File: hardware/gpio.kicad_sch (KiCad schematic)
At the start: 13 parts, among them U4 CCGM1A1

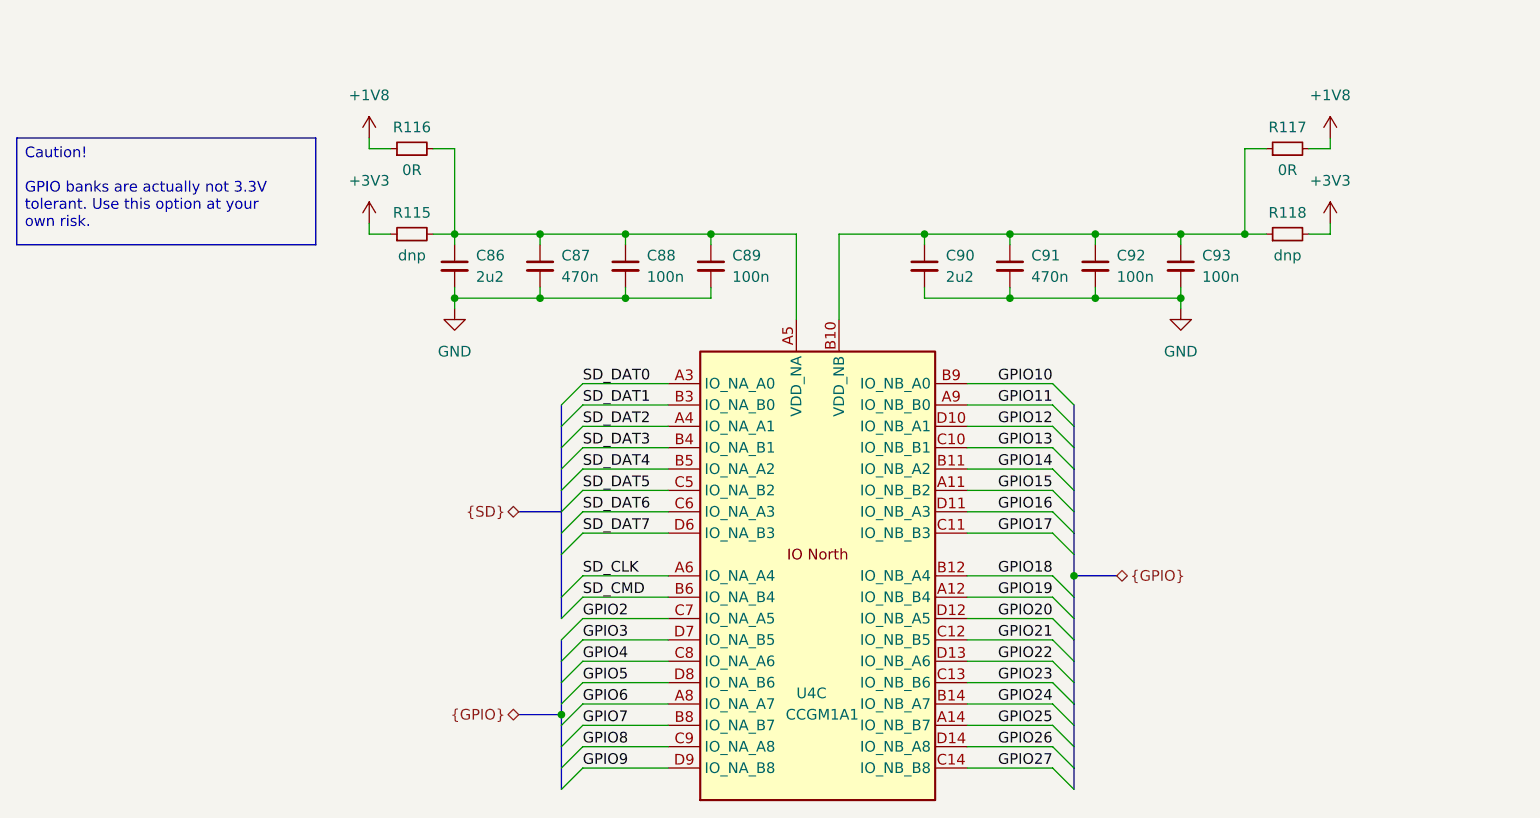
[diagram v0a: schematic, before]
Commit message: Using high SDcard pins for SDRAM
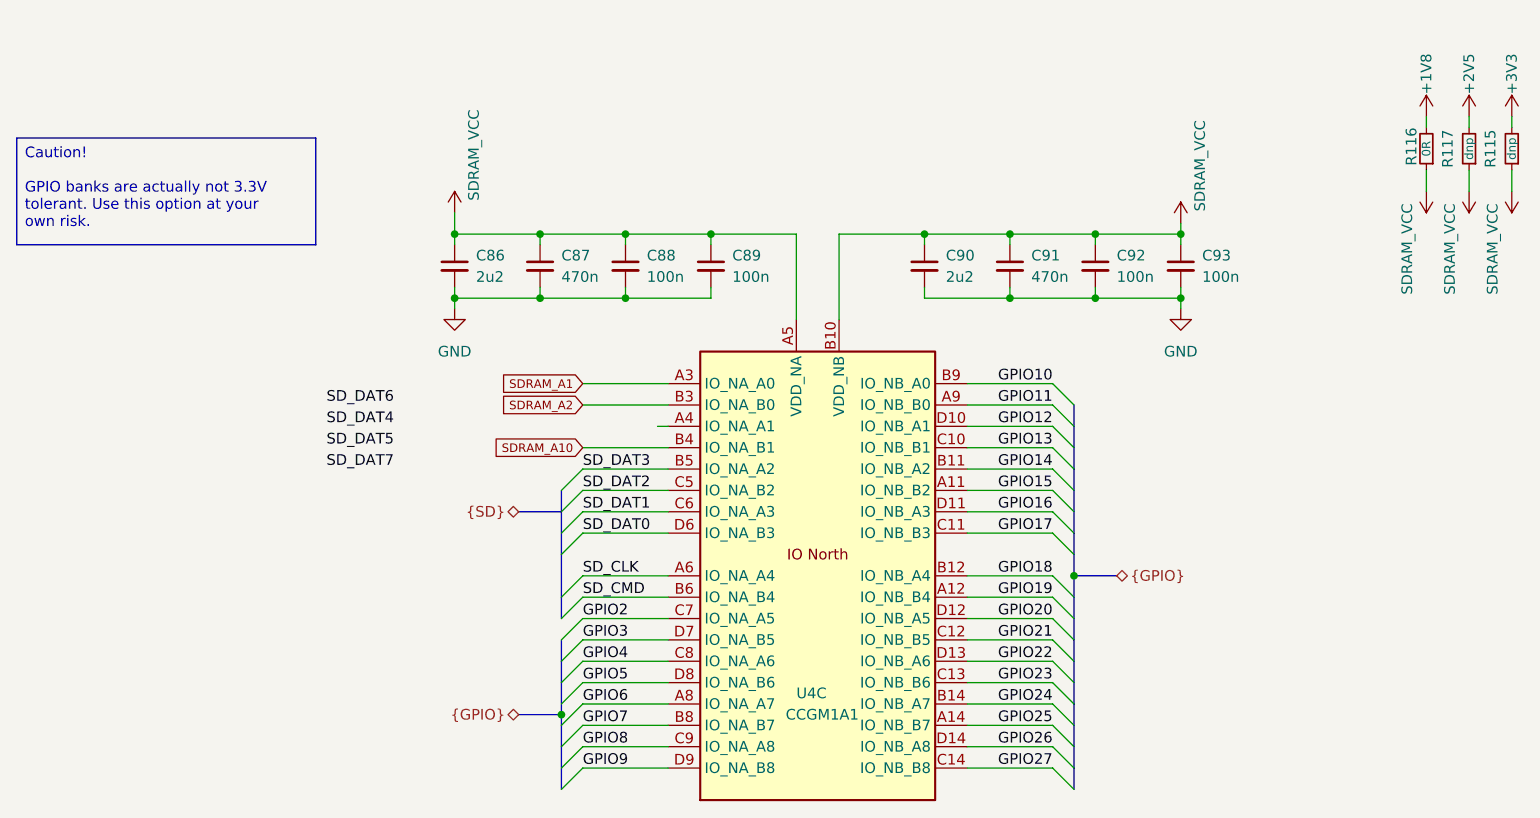
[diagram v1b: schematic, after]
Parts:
- removed R118: dnp, Resistor_SMD:R_0402_1005Metric, symbol Device:R_Small
- R117: value 0R -> dnp
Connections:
- net +1V8: now also R116.2; no longer R116.1, R117.2
- net +3V3: now also R115.2; no longer R115.1
- net SD_DAT0: now also U4.D6 (IO_NA_B3); no longer U4.A3 (IO_NA_A0)
- net SD_DAT1: now also U4.C6 (IO_NA_A3); no longer U4.B3 (IO_NA_B0)
- net SD_DAT2: now also U4.C5 (IO_NA_B2); no longer U4.A4 (IO_NA_A1)
- net SD_DAT3: now also U4.B5 (IO_NA_A2); no longer U4.B4 (IO_NA_B1)
- net SD_DAT4: no longer U4.B5 (IO_NA_A2)
- net SD_DAT5: no longer U4.C5 (IO_NA_B2)
- net SD_DAT6: no longer U4.C6 (IO_NA_A3)
- net SD_DAT7: no longer U4.D6 (IO_NA_B3)
- net SDRAM_VCC: now reaches C90.1, C91.1, C92.1, C93.1, R117.1, U4.B10 (VDD_NB), U4.B13 (VDD_NB), U4.E10 (VDD_NB), U4.E12 (VDD_NB), U4.F11 (VDD_NB)
- net SDRAM_VCC: now also C86.1, C87.1, C88.1, C89.1, R115.1, R116.1, U4.A5 (VDD_NA), U4.B7 (VDD_NA), U4.E6 (VDD_NA), U4.E8 (VDD_NA), U4.F7 (VDD_NA)
- new net +2V5: R117.2
- new net SDRAM_A1: U4.A3 (IO_NA_A0)
- new net SDRAM_A10: U4.B4 (IO_NA_B1)
- new net SDRAM_A2: U4.B3 (IO_NA_B0)
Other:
- moved on the sheet: R115, R116

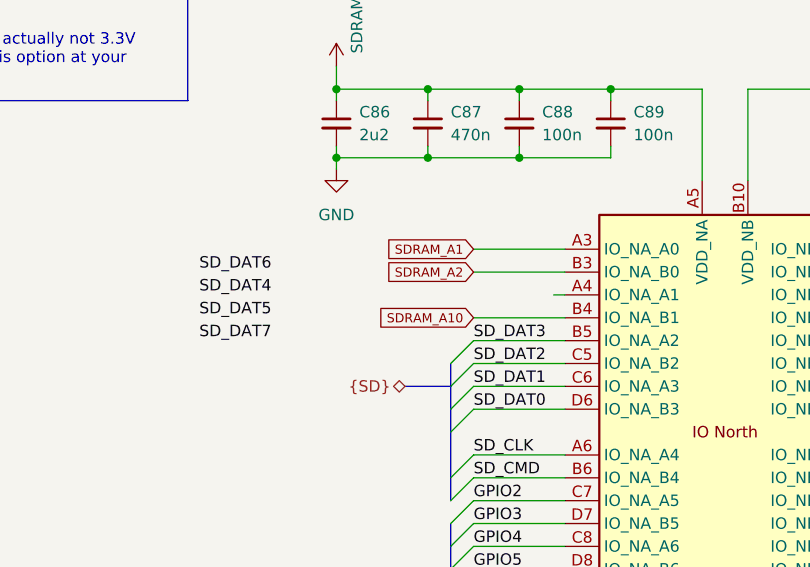
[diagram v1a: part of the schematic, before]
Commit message: Adding USB connector and level converter
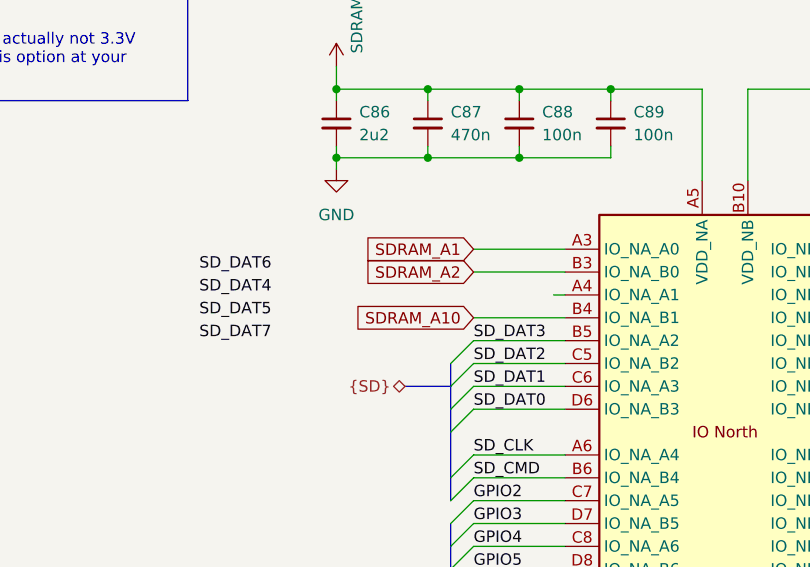
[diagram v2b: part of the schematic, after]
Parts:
- U4: footprint Package_BGA:BGA-324_15.0x15.0mm_Layout18x18_P0.8mm_Ball0.45mm_Pad0.4mm_NSMD -> ulx5m-gs:BGA-324_15.0x15.0mm_Layout18x18_P0.8mm_Ball0.45mm_Pad0.4mm_NSMD
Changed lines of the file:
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@@
 		(effects
 			(font
-				(size 1.016 1.016)
+				(size 1.27 1.27)
 			)
 			(justify right)
@@
 		(effects
 			(font
-				(size 1.016 1.016)
+				(size 1.27 1.27)
 			)
 			(justify right)
@@
 		(effects
 			(font
-				(size 1.016 1.016)
+				(size 1.27 1.27)
 			)
 			(justify right)
@@
 			)
 		)
-		(property "Footprint" "Package_BGA:BGA-324_15.0x15.0mm_Layout18x18_P0.8mm_Ball0.45mm_Pad0.4mm_NSMD"
+		(property "Footprint" "ulx5m-gs:BGA-324_15.0x15.0mm_Layout18x18_P0.8mm_Ball0.45mm_Pad0.4mm_NSMD"
 			(at 147.32 62.23 0)
 			(effects

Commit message: Routing diff clock
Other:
- company: (none) -> ${project_creator}
- title: (none) -> ${project_name}
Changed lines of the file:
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@@
 	(generator_version "9.0")
 	(paper "A4")
+	(title_block
+		(title "${project_name}")
+		(date "2025-06-24")
+		(rev "${project_version}")
+		(company "${project_creator}")
+		(comment 1 "${project_license}")
+	)
 	(text_box "Caution!\n\nGPIO banks are actually not 3.3V tolerant. Use this option at your own risk."
 		(exclude_from_sim no)

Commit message: Clearing errors
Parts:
- added R126, R127: 4R7, Resistor_SMD:R_0402_1005Metric, symbol Device:R_Small
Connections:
- net SDRAM_VCC: now also R126.1, R127.2; no longer C87.1, C88.1, C89.1, C90.1, C91.1, C92.1, U4.A5 (VDD_NA), U4.B10 (VDD_NB), U4.B13 (VDD_NB), U4.B7 (VDD_NA), U4.E10 (VDD_NB), U4.E12 (VDD_NB), U4.E6 (VDD_NA), U4.E8 (VDD_NA), U4.F11 (VDD_NB), U4.F7 (VDD_NA)
- new net VCC_NA: C87.1, C88.1, C89.1, R126.2, U4.A5 (VDD_NA), U4.B7 (VDD_NA), U4.E6 (VDD_NA), U4.E8 (VDD_NA), U4.F7 (VDD_NA)
- new net VCC_NB: C90.1, C91.1, C92.1, R127.1, U4.B10 (VDD_NB), U4.B13 (VDD_NB), U4.E10 (VDD_NB), U4.E12 (VDD_NB), U4.F11 (VDD_NB)
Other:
- moved on the sheet: R115, R116, R117

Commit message: Routing GPIO
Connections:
- net GPIO10: now also U4.C10 (IO_NB_B1); no longer U4.B9 (IO_NB_A0)
- net GPIO11: now also U4.C11 (IO_NB_B3); no longer U4.A9 (IO_NB_B0)
- net GPIO12: now also U4.A12 (IO_NB_B4); no longer U4.D10 (IO_NB_A1)
- net GPIO13: now also U4.D13 (IO_NB_A6); no longer U4.C10 (IO_NB_B1)
- net GPIO14: now also U4.A6 (IO_NA_A4); no longer U4.B11 (IO_NB_A2)
- net GPIO15: now also U4.B6 (IO_NA_B4); no longer U4.A11 (IO_NB_B2)
- net GPIO16: now also U4.B12 (IO_NB_A4); no longer U4.D11 (IO_NB_A3)
- net GPIO17: now also U4.C8 (IO_NA_A6); no longer U4.C11 (IO_NB_B3)
- net GPIO18: now also U4.A8 (IO_NA_A7); no longer U4.B12 (IO_NB_A4)
- net GPIO19: now also U4.C14 (IO_NB_B8); no longer U4.A12 (IO_NB_B4)
- net GPIO2: now also U4.D7 (IO_NA_B5); no longer U4.C7 (IO_NA_A5)
- net GPIO20: now also U4.A14 (IO_NB_B7); no longer U4.D12 (IO_NB_A5)
- net GPIO21: now also U4.B14 (IO_NB_A7); no longer U4.C12 (IO_NB_B5)
- net GPIO22: now also U4.D9 (IO_NA_B8); no longer U4.D13 (IO_NB_A6)
- net GPIO23: now also U4.B8 (IO_NA_B7); no longer U4.C13 (IO_NB_B6)
- net GPIO24: now also U4.A9 (IO_NB_B0); no longer U4.B14 (IO_NB_A7)
- net GPIO25: now also U4.B9 (IO_NB_A0); no longer U4.A14 (IO_NB_B7)
- net GPIO27: now also U4.C9 (IO_NA_A8); no longer U4.C14 (IO_NB_B8)
- net GPIO3: now also U4.C7 (IO_NA_A5); no longer U4.D7 (IO_NA_B5)
- net GPIO4: now also U4.D8 (IO_NA_B6); no longer U4.C8 (IO_NA_A6)
- net GPIO5: now also U4.C12 (IO_NB_B5); no longer U4.D8 (IO_NA_B6)
- net GPIO6: now also U4.C13 (IO_NB_B6); no longer U4.A8 (IO_NA_A7)
- net GPIO7: now also U4.B11 (IO_NB_A2); no longer U4.B8 (IO_NA_B7)
- net GPIO8: now also U4.A11 (IO_NB_B2); no longer U4.C9 (IO_NA_A8)
- net GPIO9: now also U4.D10 (IO_NB_A1); no longer U4.D9 (IO_NA_B8)
- net SD_CLK: now also U4.C6 (IO_NA_A3); no longer U4.A6 (IO_NA_A4)
- net SD_CMD: now also U4.D6 (IO_NA_B3); no longer U4.B6 (IO_NA_B4)
- net SD_DAT0: now also U4.A4 (IO_NA_A1); no longer U4.D6 (IO_NA_B3)
- net SD_DAT1: now also U4.D12 (IO_NB_A5); no longer U4.C6 (IO_NA_A3)
- new net ID_SD: U4.D11 (IO_NB_A3)

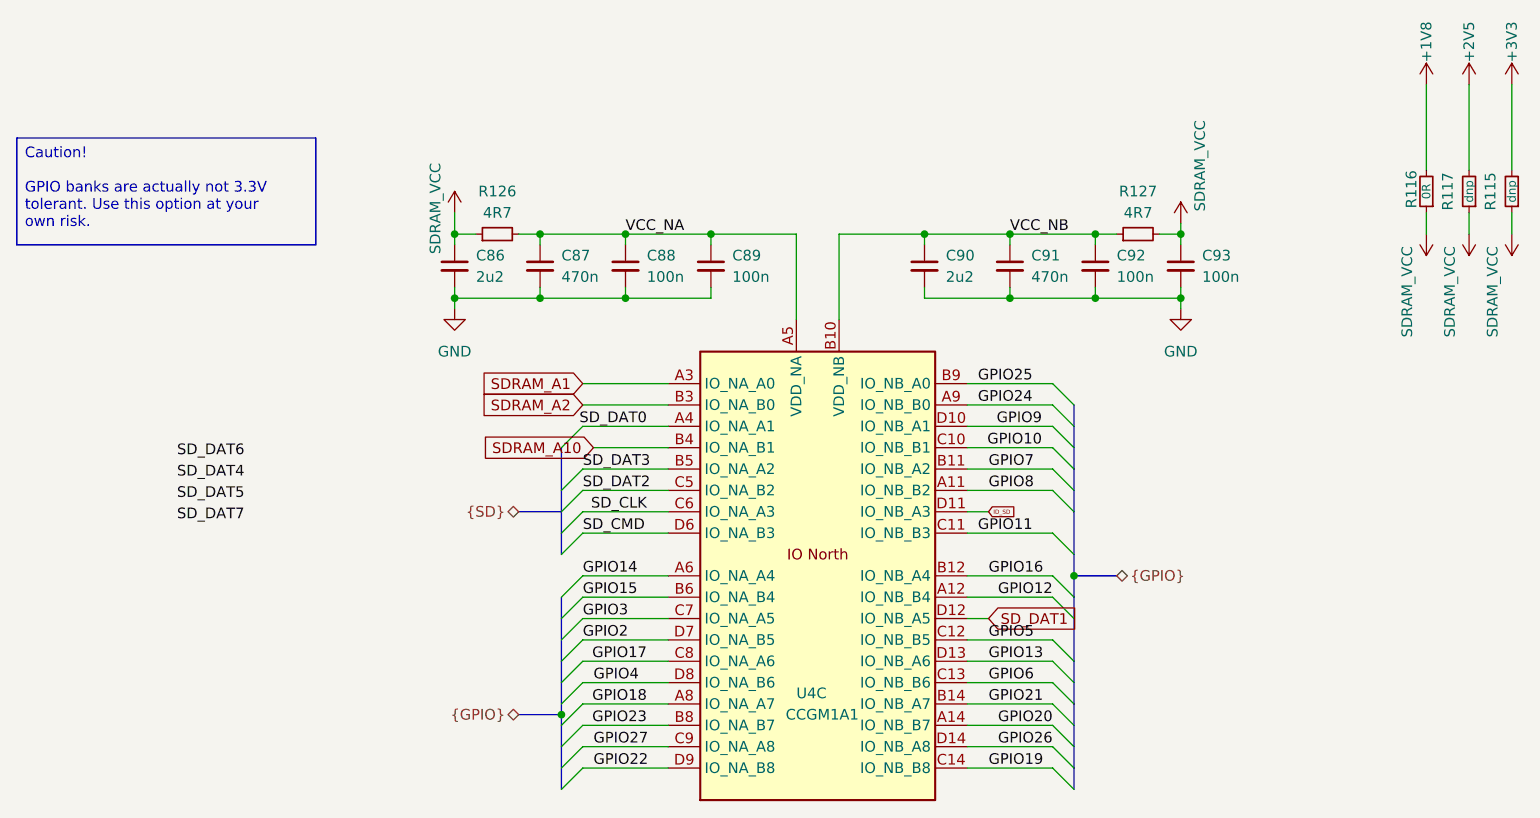
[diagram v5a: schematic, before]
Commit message: Routing GPDI
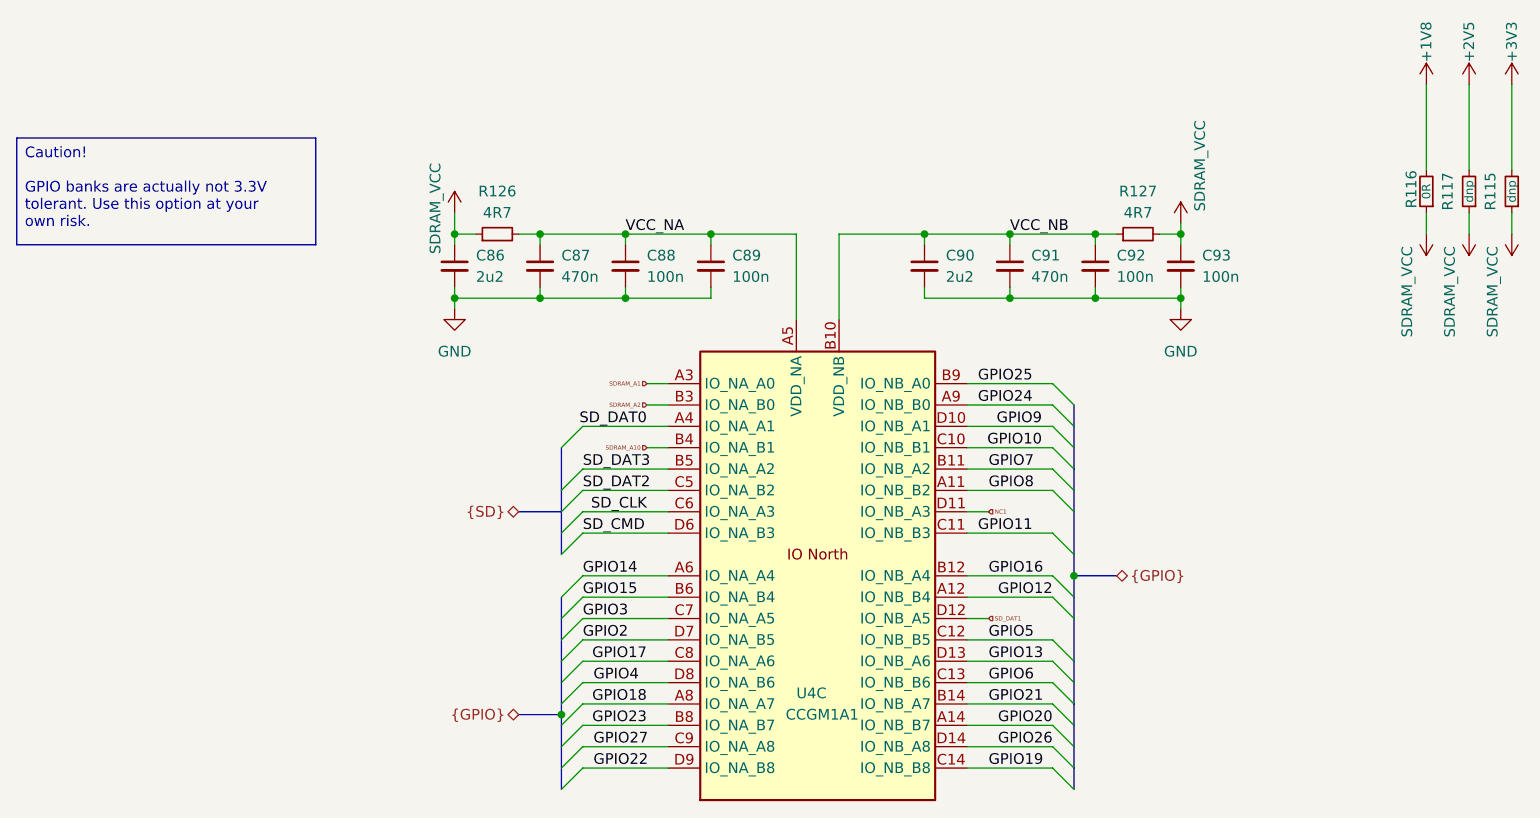
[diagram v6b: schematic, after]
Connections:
- net ID_SD renamed NC1
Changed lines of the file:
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@@
 	(wire
 		(pts
-			(xy 125.73 63.5) (xy 134.62 63.5)
+			(xy 132.08 63.5) (xy 134.62 63.5)
 		)
 		(stroke
@@
 	(wire
 		(pts
-			(xy 124.46 55.88) (xy 134.62 55.88)
+			(xy 132.08 55.88) (xy 134.62 55.88)
 		)
 		(stroke
@@
 	(wire
 		(pts
-			(xy 124.46 58.42) (xy 134.62 58.42)
+			(xy 132.08 58.42) (xy 134.62 58.42)
 		)
 		(stroke
@@
 		)
 	)
-	(label "SD_DAT5"
-		(at 76.2 69.85 0)
-		(effects
-			(font
-				(size 1.27 1.27)
-			)
-			(justify left bottom)
-		)
-	)
 	(label "SD_DAT3"
 		(at 124.46 66.04 0)
@@
 		)
 	)
-	(label "SD_DAT7"
-		(at 76.2 72.39 0)
-		(effects
-			(font
-				(size 1.27 1.27)
-			)
-			(justify left bottom)
-		)
-	)
 	(label "VCC_NA"
 		(at 129.54 38.1 0)
@@
 		)
 	)
-	(label "SD_DAT6"
-		(at 76.2 64.77 0)
-		(effects
-			(font
-				(size 1.27 1.27)
-			)
-			(justify left bottom)
-		)
-	)
 	(label "GPIO25"
 		(at 171.45 55.88 0)
@@
 		)
 	)
-	(label "SD_DAT4"
-		(at 76.2 67.31 0)
-		(effects
-			(font
-				(size 1.27 1.27)
-			)
-			(justify left bottom)
-		)
-	)
 	(label "GPIO2"
 		(at 124.46 86.36 0)
@@
 			)
 			(justify right bottom)
-		)
-	)
-	(global_label "SDRAM_A10"
-		(shape input)
-		(at 125.73 63.5 180)
-		(effects
-			(font
-				(size 1.27 1.27)
-			)
-			(justify right)
-		)
-		(property "Intersheetrefs" "${INTERSHEET_REFS}"
-			(at 125.73 63.5 0)
-			(effects
-				(font
-					(size 1.27 1.27)
-				)
-				(hide yes)
-			)
-		)
-	)
-	(global_label "SD_DAT1"
-		(shape input)
-		(at 172.72 83.82 0)
-		(fields_autoplaced yes)
-		(effects
-			(font
-				(size 1.27 1.27)
-			)
-			(justify left)
-		)
-		(property "Intersheetrefs" "${INTERSHEET_REFS}"
-			(at 183.688 83.82 0)
-			(effects
-				(font
-					(size 1.27 1.27)
-				)
-				(justify left)
-				(hide yes)
-			)
-		)
-	)
-	(global_label "SDRAM_A2"
-		(shape input)
-		(at 124.46 58.42 180)
-		(effects
-			(font
-				(size 1.27 1.27)
-			)
-			(justify right)
-		)
-		(property "Intersheetrefs" "${INTERSHEET_REFS}"
-			(at 124.46 58.42 0)
-			(effects
-				(font
-					(size 1.27 1.27)
-				)
-				(hide yes)
-			)
-		)
-	)
-	(global_label "ID_SD"
-		(shape input)
-		(at 172.72 71.12 0)
-		(fields_autoplaced yes)
-		(effects
-			(font
-				(size 0.5 0.5)
-			)
-			(justify left)
-		)
-		(property "Intersheetrefs" "${INTERSHEET_REFS}"
-			(at 175.9906 71.12 0)
-			(effects
-				(font
-					(size 1.27 1.27)
-				)
-				(justify left)
-				(hide yes)
-			)
-		)
-	)
-	(global_label "SDRAM_A1"
-		(shape input)
-		(at 124.46 55.88 180)
-		(effects
-			(font
-				(size 1.27 1.27)
-			)
-			(justify right)
-		)
-		(property "Intersheetrefs" "${INTERSHEET_REFS}"
-			(at 124.46 55.88 0)
-			(effects
-				(font
-					(size 1.27 1.27)
-				)
-				(hide yes)
-			)
 		)
 	)
@@
 		)
 	)
+	(hierarchical_label "SDRAM_A10"
+		(shape input)
+		(at 132.08 63.5 180)
+		(effects
+			(font
+				(size 0.5 0.5)
+			)
+			(justify right)
+		)
+	)
+	(hierarchical_label "SDRAM_A2"
+		(shape input)
+		(at 132.08 58.42 180)
+		(effects
+			(font
+				(size 0.5 0.5)
+			)
+			(justify right)
+		)
+	)
+	(hierarchical_label "SD_DAT1"
+		(shape input)
+		(at 172.72 83.82 0)
+		(effects
+			(font
+				(size 0.5 0.5)
+			)
+			(justify left)
+		)
+	)
+	(hierarchical_label "SDRAM_A1"
+		(shape input)
+		(at 132.08 55.88 180)
+		(effects
+			(font
+				(size 0.5 0.5)
+			)
+			(justify right)
+		)
+	)
 	(hierarchical_label "{GPIO}"
 		(shape bidirectional)
@@
 			)
 			(justify left)
+		)
+	)
+	(hierarchical_label "NC1"
+		(shape input)
+		(at 172.72 71.12 0)
+		(effects
+			(font
+				(size 0.5 0.5)
+			)
+			(justify left)
